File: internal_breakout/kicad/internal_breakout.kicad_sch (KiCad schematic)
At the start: 27 parts, among them J1 MA03-1, J10 2X5, J11 2X5, J12 MA03-1, J13 MA03-1, J14 MA03-1, J15 MA03-1, J16 MA03-1, J17 MA03-1, J18 Conn_02x01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

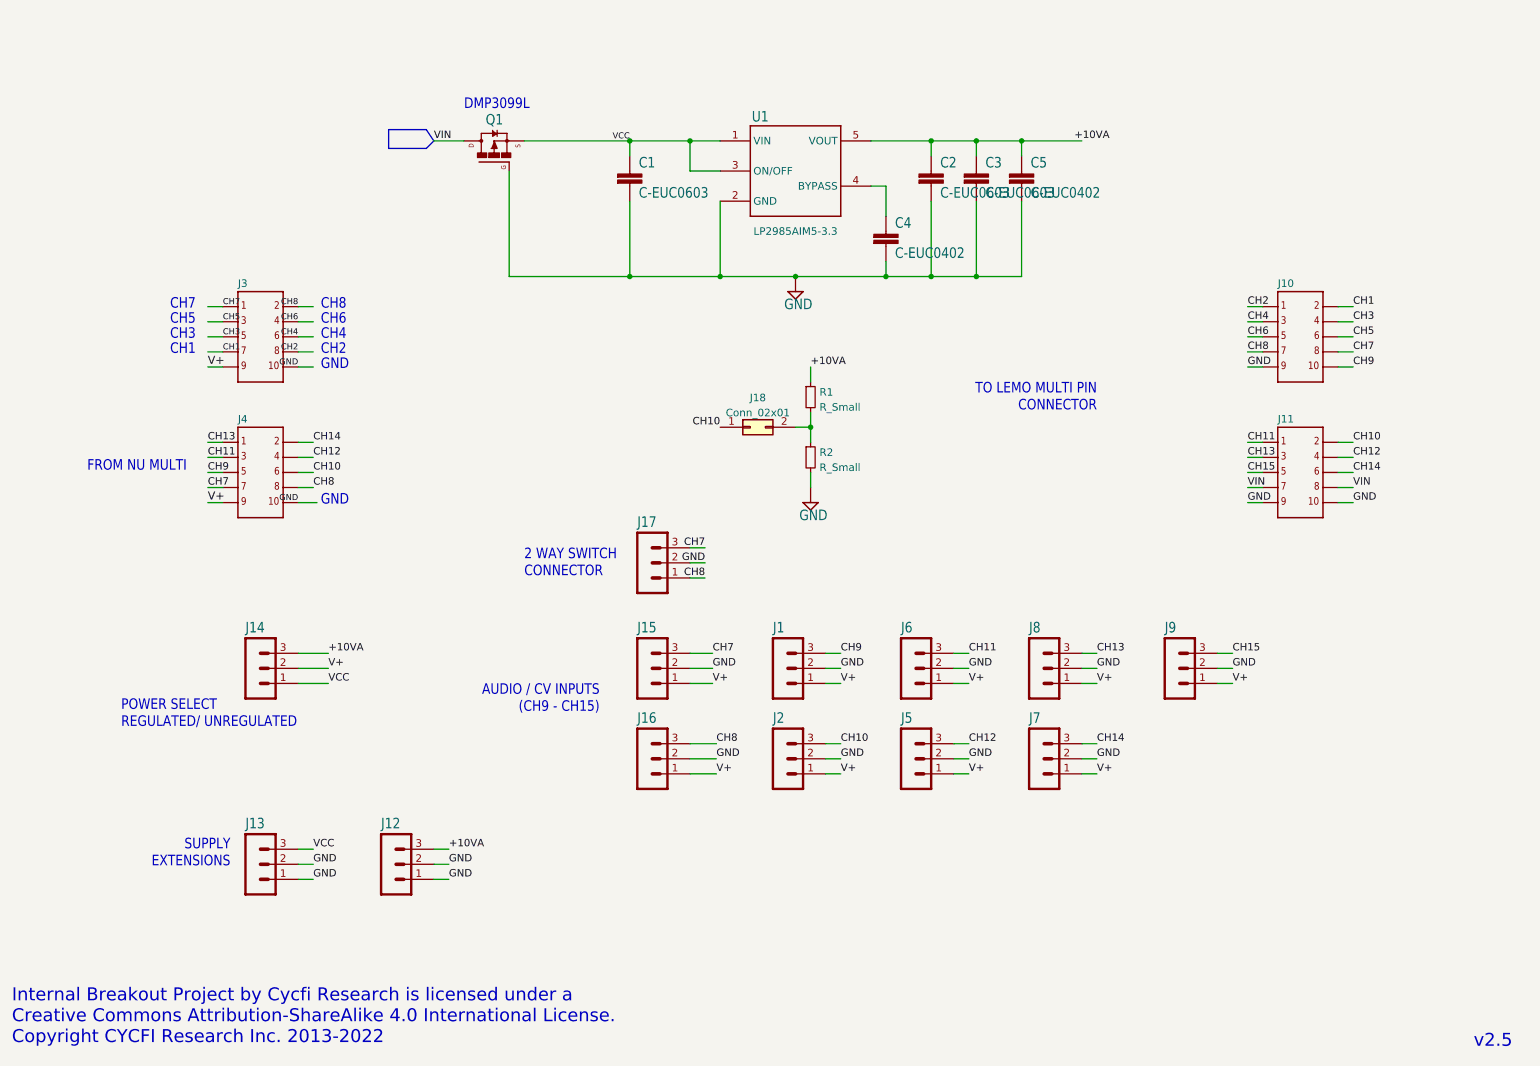
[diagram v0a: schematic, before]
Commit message: Perfect port to KiCAD
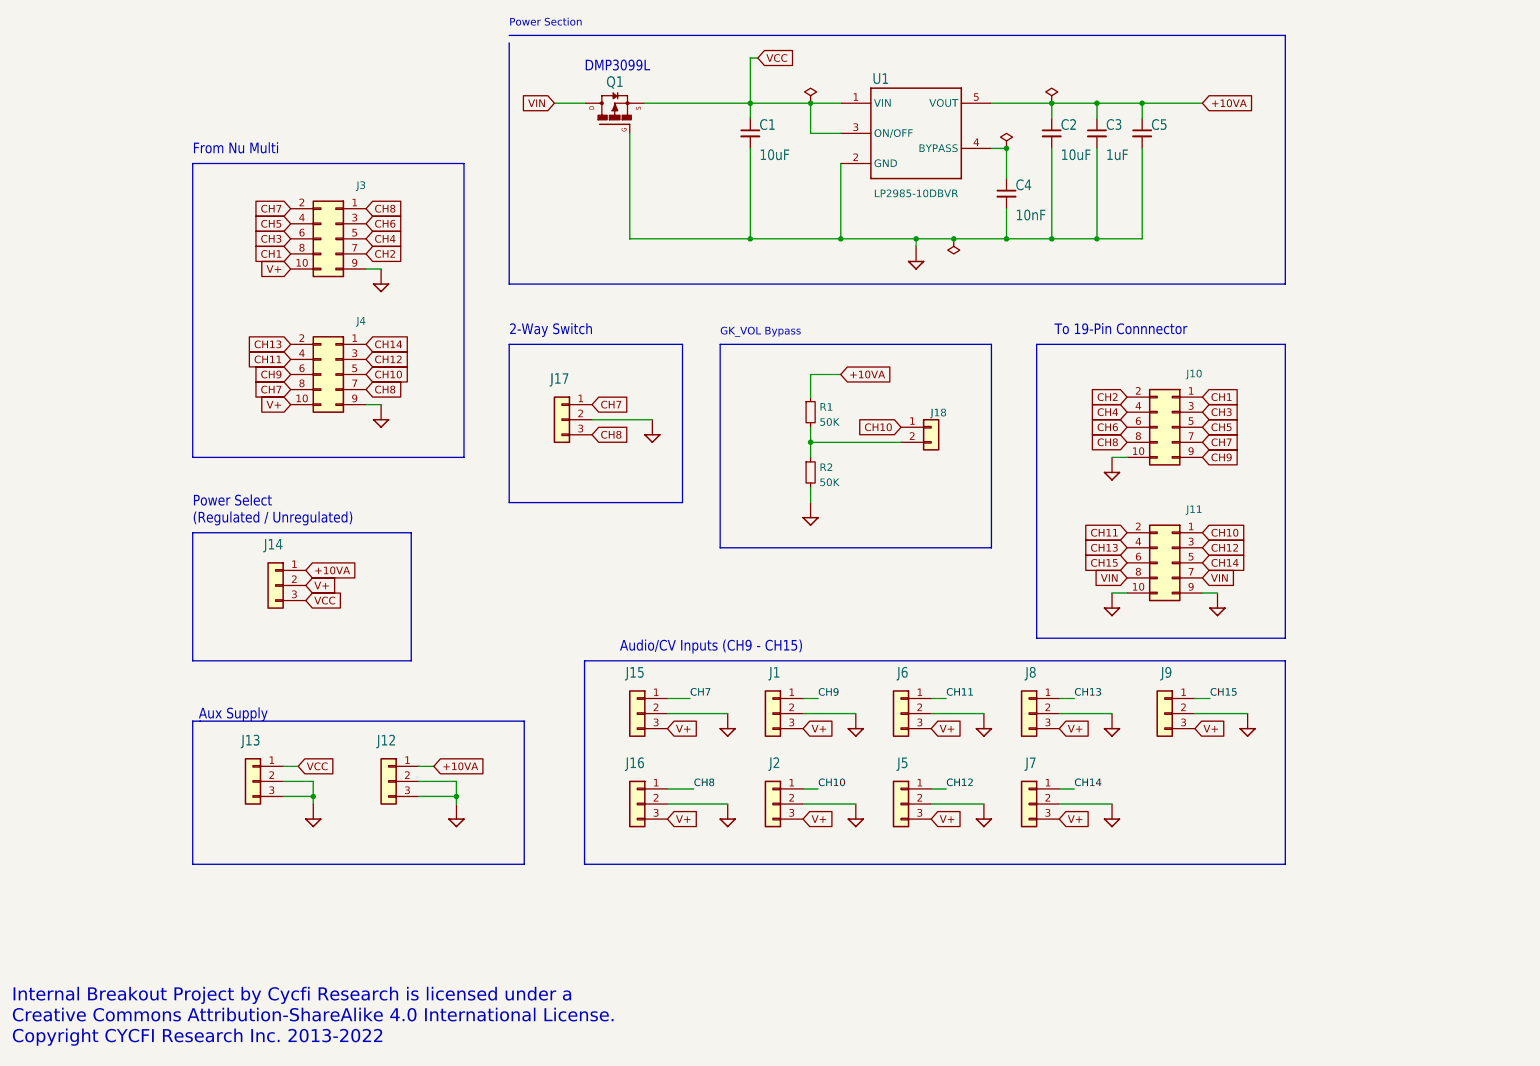
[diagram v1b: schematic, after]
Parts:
- C1, C2: value C-EUC0603 -> 10uF; footprint internal_breakout:C0603 -> Capacitor_SMD:C_0603_1608Metric; symbol internal_breakout-eagle-import:C-EUC0603 -> Device:C_Small
- C3: value C-EUC0603 -> 1uF; footprint internal_breakout:C0603 -> Capacitor_SMD:C_0603_1608Metric; symbol internal_breakout-eagle-import:C-EUC0603 -> Device:C_Small
- C4: value C-EUC0402 -> 10nF; footprint internal_breakout:C0402 -> Capacitor_SMD:C_0402_1005Metric; symbol internal_breakout-eagle-import:C-EUC0402 -> Device:C_Small
- C5: value C-EUC0402 -> 100nF; footprint internal_breakout:C0402 -> Capacitor_SMD:C_0402_1005Metric; symbol internal_breakout-eagle-import:C-EUC0402 -> Device:C_Small
- J1, J12, J13, J14, J2, J5, J6, J7, J8, J9: footprint Connector_PinHeader_2.00mm:PinHeader_1x03_P2.00mm_Vertical -> Connector_PinHeader_2.54mm:PinHeader_1x03_P2.54mm_Vertical; symbol internal_breakout-eagle-import:MA03-1 -> Connector_Generic:Conn_01x03
- J10, J11, J3, J4: footprint internal_breakout:2X5 -> Connector_PinHeader_2.00mm:PinHeader_2x05_P2.00mm_Vertical; symbol internal_breakout-eagle-import:2X5 -> Connector_Generic:Conn_02x05_Odd_Even
- J15, J16, J17: value MA03-1 -> Conn_01x03; footprint Connector_PinHeader_2.00mm:PinHeader_1x03_P2.00mm_Vertical -> Connector_PinHeader_2.54mm:PinHeader_1x03_P2.54mm_Vertical; symbol internal_breakout-eagle-import:MA03-1 -> Connector_Generic:Conn_01x03
- J18: symbol Connector_Generic:Conn_02x01 -> Connector_Generic:Conn_01x02
- R1, R2: value R_Small -> 50K
- U1: value LP2985AIM5-3.3 -> LP2985-10DBVR
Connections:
- net +10VA: now also J12.1 (Pin_1), J14.1 (Pin_1); no longer J12.3, J14.3
- net CH1: now also J10.1 (Pin_1), J3.8 (Pin_8); no longer J10.2, J3.7
- net CH10: now also J11.1 (Pin_1), J2.1 (Pin_1), J4.5 (Pin_5); no longer J11.2, J2.3, J4.6
- net CH11: now also J11.2 (Pin_2), J4.4 (Pin_4), J6.1 (Pin_1); no longer J11.1, J4.3, J6.3
- net CH12: now also J11.3 (Pin_3), J4.3 (Pin_3), J5.1 (Pin_1); no longer J11.4, J4.4, J5.3
- net CH13: now also J11.4 (Pin_4), J4.2 (Pin_2), J8.1 (Pin_1); no longer J11.3, J4.1, J8.3
- net CH14: now also J11.5 (Pin_5), J4.1 (Pin_1), J7.1 (Pin_1); no longer J11.6, J4.2, J7.3
- net CH15: now also J11.6 (Pin_6), J9.1 (Pin_1); no longer J11.5, J9.3
- net CH2: now also J10.2 (Pin_2), J3.7 (Pin_7); no longer J10.1, J3.8
- net CH3: now also J10.3 (Pin_3), J3.6 (Pin_6); no longer J10.4, J3.5
- net CH4: now also J10.4 (Pin_4), J3.5 (Pin_5); no longer J10.3, J3.6
- net CH5: now also J10.5 (Pin_5), J3.4 (Pin_4); no longer J10.6, J3.3
- net CH6: now also J10.6 (Pin_6), J3.3 (Pin_3); no longer J10.5, J3.4
- net CH7: now also J10.7 (Pin_7), J15.1 (Pin_1), J17.1 (Pin_1), J3.2 (Pin_2), J4.8 (Pin_8); no longer J10.8, J15.3, J17.3, J3.1, J4.7
- net CH8: now also J10.8 (Pin_8), J16.1 (Pin_1), J17.3 (Pin_3), J3.1 (Pin_1), J4.7 (Pin_7); no longer J10.7, J16.3, J17.1, J3.2, J4.8
- net CH9: now also J1.1 (Pin_1), J10.9 (Pin_9), J4.6 (Pin_6); no longer J1.3, J10.10, J4.5
- net GND: now also J10.10 (Pin_10), J12.3 (Pin_3), J13.3 (Pin_3), J3.9 (Pin_9), J4.9 (Pin_9); no longer J10.9, J12.1, J13.1, J3.10, J4.10
- net V+: now also J1.3 (Pin_3), J15.3 (Pin_3), J16.3 (Pin_3), J2.3 (Pin_3), J3.10 (Pin_10), J4.10 (Pin_10), J5.3 (Pin_3), J6.3 (Pin_3), J7.3 (Pin_3), J8.3 (Pin_3), J9.3 (Pin_3); no longer J1.1, J15.1, J16.1, J2.1, J3.9, J4.9, J5.1, J6.1, J7.1, J8.1, J9.1
- net VCC: now also J13.1 (Pin_1), J14.3 (Pin_3); no longer J13.3, J14.1
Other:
- note added: "2-Way Switch"
- note added: "Audio/CV Inputs (CH9 - CH15)"
- note added: "Aux Supply"
- note added: "From Nu Multi"
- note added: "GK_VOL Bypass"
- note added: "Power Section"
- note added: "Power Select (Regulated / Unregulated)"
- note added: "To 19-Pin Connnector"
- note removed: "2 WAY SWITCH CONNECTOR"
- note removed: "AUDIO / CV INPUTS (CH9 - CH15)"
- note removed: "CH1"
- note removed: "CH2"
- note removed: "CH3"
- note removed: "CH4"
- note removed: "CH5"
- note removed: "CH6"
- note removed: "CH7"
- note removed: "CH8"
- note removed: "FROM NU MULTI"
- note removed: "GND"
- note removed: "POWER SELECT REGULATED/ UNREGULATED"
- note removed: "SUPPLY EXTENSIONS"
- note removed: "TO LEMO MULTI PIN CONNECTOR"
- note removed: "v2.5"
- moved on the sheet: J18, Q1, R1, R2, U1

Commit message: LCSC part numbers
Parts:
- added C6: 1uF, Capacitor_SMD:C_0402_1005Metric, symbol Device:C_Small
- C1, C2: LCSC (none) -> C96446
- C3: footprint Capacitor_SMD:C_0603_1608Metric -> Capacitor_SMD:C_0402_1005Metric; LCSC (none) -> C52923
- C4: LCSC (none) -> C15195
- C5: LCSC (none) -> C307331
- Q1: value FDN360P -> DMP3099L-7; LCSC (none) -> C558116
- R1, R2: value 50K -> 47K; LCSC (none) -> C25792
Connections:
- net GND: now also C6.2
- net at J18.2 (Pin_2), R1.2, R2.1: now also C6.1
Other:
- note removed: "DMP3099L"
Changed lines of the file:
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@@
   (junction (at 160.02 88.9) (diameter 0) (color 0 0 0 0)
   )
+  (junction (at 170.18 88.9) (diameter 0) (color 0 0 0 0)
+  )
   (junction (at 215.9 31.75) (diameter 0) (color 0 0 0 0)
   )
@@
     (stroke (width 0) (type default) (color 0 0 0 0))
   )
+  (wire (pts (xy 170.18 88.9) (xy 175.26 88.9))
+    (stroke (width 0) (type default) (color 0 0 0 0))
+  )
   (wire (pts (xy 201.93 134.62) (xy 210.82 134.62))
     (stroke (width 0) (type default) (color 0 0 0 0))
@@
     (stroke (width 0) (type default) (color 0 0 0 0))
   )
-  (wire (pts (xy 160.02 88.9) (xy 175.26 88.9))
+  (wire (pts (xy 160.02 88.9) (xy 170.18 88.9))
     (stroke (width 0) (type default) (color 0 0 0 0))
   )
@@
     (stroke (width 0) (type default) (color 0 0 0 0))
   )
+  (wire (pts (xy 170.18 88.9) (xy 170.18 91.44))
+    (stroke (width 0) (type default) (color 0 0 0 0))
+  )
   (wire (pts (xy 200.66 31.75) (xy 208.28 31.75))
     (stroke (width 0) (type default) (color 0 0 0 0))
@@
   )
   (wire (pts (xy 213.36 114.3) (xy 210.82 114.3))
+    (stroke (width 0) (type default) (color 0 0 0 0))
+  )
+  (wire (pts (xy 170.18 96.52) (xy 170.18 99.06))
     (stroke (width 0) (type default) (color 0 0 0 0))
   )
@@
   )
   (text "Power Section" (at 109.22 19.05 0)
-    (effects (font (size 1.27 1.27)) (justify left bottom))
+    (effects (font (size 1.5113 1.5113)) (justify left bottom))
   )
   (text "Audio/CV Inputs (CH9 - CH15)" (at 158.75 124.46 180)
@@
     (effects (font (size 2.1844 2.1844)) (justify left bottom))
   )
-  (text "DMP3099L" (at 121.92 26.67 180)
-    (effects (font (size 1.778 1.5113)) (justify left bottom))
-  )
   (text "To 19-Pin Connnector" (at 223.52 71.12 180)
     (effects (font (size 1.778 1.5113)) (justify right bottom))
@@
     )
     (pin "1")
+  )
+  (symbol (lib_id "Device:C_Small") (at 170.18 93.98 0) (unit 1)
+    (in_bom yes) (on_board yes)
+    (property "Reference" "C6" (id 0) (at 171.704 93.599 0)
+      (effects (font (size 1.778 1.5113)) (justify left bottom))
+    )
+    (property "Value" "1uF" (id 1) (at 171.704 98.679 0)
+      (effects (font (size 1.778 1.5113)) (justify left bottom))
+    )
+    (property "Footprint" "Capacitor_SMD:C_0402_1005Metric" (id 2) (at 170.18 93.98 0)
+      (effects (font (size 1.27 1.27)) hide)
+    )
+    (property "Datasheet" "~" (id 3) (at 170.18 93.98 0)
+      (effects (font (size 1.27 1.27)) hide)
+    )
+    (property "LCSC" "C52923" (id 4) (at 170.18 93.98 0)
+      (effects (font (size 1.27 1.27)) hide)
+    )
+    (pin "1")
+    (pin "2")
   )
   (symbol (lib_id "Connector_Generic:Conn_02x05_Odd_Even") (at 220.98 109.22 0) (mirror y) (unit 1)
@@
       (effects (font (size 1.27 1.27)) hide)
     )
+    (property "LCSC" "C307331" (id 4) (at 215.9 36.83 0)
+      (effects (font (size 1.27 1.27)) hide)
+    )
     (pin "1")
     (pin "2")
@@
     )
     (property "Datasheet" "~" (id 3) (at 200.66 36.83 0)
+      (effects (font (size 1.27 1.27)) hide)
+    )
+    (property "LCSC" "C96446" (id 4) (at 200.66 36.83 0)
       (effects (font (size 1.27 1.27)) hide)
     )
@@
       (effects (font (size 1.778 1.5113)) (justify left bottom))
     )
-    (property "Footprint" "Capacitor_SMD:C_0603_1608Metric" (id 2) (at 208.28 36.83 0)
+    (property "Footprint" "Capacitor_SMD:C_0402_1005Metric" (id 2) (at 208.28 36.83 0)
       (effects (font (size 1.27 1.27)) hide)
     )
@@
       (effects (font (size 1.27 1.27)) hide)
     )
+    (property "LCSC" "C52923" (id 4) (at 208.28 36.83 0)
+      (effects (font (size 1.27 1.27)) hide)
+    )
     (pin "1")
     (pin "2")
@@
     )
     (property "Datasheet" "~" (id 3) (at 149.86 36.83 0)
+      (effects (font (size 1.27 1.27)) hide)
+    )
+    (property "LCSC" "C96446" (id 4) (at 149.86 36.83 0)
       (effects (font (size 1.27 1.27)) hide)
     )
@@
       (effects (font (size 1.27 1.27)) hide)
     )
+    (property "LCSC" "C15195" (id 4) (at 193.04 46.99 0)
+      (effects (font (size 1.27 1.27)) hide)
+    )
     (pin "1")
     (pin "2")
@@
       (effects (font (size 1.27 1.27)) (justify left))
     )
-    (property "Value" "50K" (id 1) (at 161.5186 85.5222 0)
+    (property "Value" "47K" (id 1) (at 161.5186 85.5222 0)
       (effects (font (size 1.27 1.27)) (justify left))
     )
@@
       (effects (font (size 1.27 1.27)) hide)
     )
+    (property "LCSC" "C25792" (id 4) (at 160.02 83.82 0)
+      (effects (font (size 1.27 1.27)) hide)
+    )
     (pin "1")
     (pin "2")
@@
     )
     (property "Datasheet" "" (id 3) (at 87.63 62.23 0)
+      (effects (font (size 1.27 1.27)) hide)
+    )
+    (pin "1")
+  )
+  (symbol (lib_id "internal_breakout-eagle-import:GND") (at 170.18 101.6 0) (unit 1)
+    (in_bom yes) (on_board yes)
+    (property "Reference" "#SUPPLY04" (id 0) (at 170.18 101.6 0)
+      (effects (font (size 1.27 1.27)) hide)
+    )
+    (property "Value" "GND" (id 1) (at 167.64 106.68 0)
+      (effects (font (size 1.778 1.5113)) (justify left bottom) hide)
+    )
+    (property "Footprint" "internal_breakout:" (id 2) (at 170.18 101.6 0)
+      (effects (font (size 1.27 1.27)) hide)
+    )
+    (property "Datasheet" "" (id 3) (at 170.18 101.6 0)
       (effects (font (size 1.27 1.27)) hide)
     )
@@
       (effects (font (size 1.778 1.5113)) (justify right top))
     )
-    (property "Value" "FDN360P" (id 1) (at 127 27.94 0)
-      (effects (font (size 1.778 1.5113)) (justify left bottom) hide)
+    (property "Value" "DMP3099L-7" (id 1) (at 115.57 38.1 90)
+      (effects (font (size 1.27 1.27)) (justify left bottom))
     )
     (property "Footprint" "Package_TO_SOT_SMD:SOT-23" (id 2) (at 127 34.29 0)
@@
     )
     (property "Datasheet" "" (id 3) (at 127 34.29 0)
+      (effects (font (size 1.27 1.27)) hide)
+    )
+    (property "LCSC" "C558116" (id 4) (at 127 34.29 0)
       (effects (font (size 1.27 1.27)) hide)
     )
@@
       (effects (font (size 1.27 1.27)) (justify left))
     )
-    (property "Value" "50K" (id 1) (at 161.5186 95.6822 0)
+    (property "Value" "47K" (id 1) (at 161.5186 95.6822 0)
       (effects (font (size 1.27 1.27)) (justify left))
     )
@@
       (effects (font (size 1.27 1.27)) hide)
     )
+    (property "LCSC" "C25792" (id 4) (at 160.02 93.98 0)
+      (effects (font (size 1.27 1.27)) hide)
+    )
     (pin "1")
     (pin "2")
@@
   (symbol (lib_id "internal_breakout-eagle-import:GND") (at 133.35 87.63 0) (unit 1)
     (in_bom yes) (on_board yes)
-    (property "Reference" "#SUPPLY?" (id 0) (at 133.35 87.63 0)
+    (property "Reference" "#SUPPLY03" (id 0) (at 133.35 87.63 0)
       (effects (font (size 1.27 1.27)) hide)
     )
@@
       (reference "#SUPPLY02") (unit 1) (value "GND") (footprint "internal_breakout:")
     )
+    (path "/f0e06de7-f83d-4848-815a-3086379a3bdb"
+      (reference "#SUPPLY03") (unit 1) (value "GND") (footprint "internal_breakout:")
+    )
+    (path "/ae7dd71c-ca1d-4baa-8bd4-5f40cd8792b3"
+      (reference "#SUPPLY04") (unit 1) (value "GND") (footprint "internal_breakout:")
+    )
     (path "/17a79149-3203-4c66-8a32-b035030f3a0d"
       (reference "#SUPPLY0101") (unit 1) (value "GND") (footprint "internal_breakout:")
@@
       (reference "#SUPPLY0116") (unit 1) (value "GND") (footprint "internal_breakout:")
     )
-    (path "/f0e06de7-f83d-4848-815a-3086379a3bdb"
-      (reference "#SUPPLY?") (unit 1) (value "GND") (footprint "internal_breakout:")
-    )
     (path "/619e5559-5c6e-40cc-87da-be0d8df0f585"
       (reference "C1") (unit 1) (value "10uF") (footprint "Capacitor_SMD:C_0603_1608Metric")
@@
     )
     (path "/5c55c653-303a-4aa1-b520-46d1ee447caa"
-      (reference "C3") (unit 1) (value "1uF") (footprint "Capacitor_SMD:C_0603_1608Metric")
+      (reference "C3") (unit 1) (value "1uF") (footprint "Capacitor_SMD:C_0402_1005Metric")
     )
     (path "/899d6960-0494-4e8f-9091-802503c02d1b"
@@
       (reference "C5") (unit 1) (value "100nF") (footprint "Capacitor_SMD:C_0402_1005Metric")
     )
+    (path "/10a7ed99-3346-4436-9e7d-492ab8b2cbc4"
+      (reference "C6") (unit 1) (value "1uF") (footprint "Capacitor_SMD:C_0402_1005Metric")
+    )
     (path "/9a68bf85-c16f-48ee-8e66-0d9ea8ea8b23"
       (reference "J1") (unit 1) (value "MA03-1") (footprint "Connector_PinHeader_2.54mm:PinHeader_1x03_P2.54mm_Vertical")
@@
     )
     (path "/b90997e2-4c7f-4479-862f-ab35dfea4f77"
-      (reference "Q1") (unit 1) (value "FDN360P") (footprint "Package_TO_SOT_SMD:SOT-23")
+      (reference "Q1") (unit 1) (value "DMP3099L-7") (footprint "Package_TO_SOT_SMD:SOT-23")
     )
     (path "/9a9b3927-c7e1-4560-999f-db27cf281135"
-      (reference "R1") (unit 1) (value "50K") (footprint "Resistor_SMD:R_0402_1005Metric")
+      (reference "R1") (unit 1) (value "47K") (footprint "Resistor_SMD:R_0402_1005Metric")
     )
     (path "/cdec2960-8356-43b8-a368-3ab4282311fc"
-      (reference "R2") (unit 1) (value "50K") (footprint "Resistor_SMD:R_0402_1005Metric")
+      (reference "R2") (unit 1) (value "47K") (footprint "Resistor_SMD:R_0402_1005Metric")
     )
     (path "/73486422-c87a-4ad4-8fe5-a3ffc70cb20a"
